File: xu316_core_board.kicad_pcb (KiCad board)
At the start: 4 copper layers, 53.3 x 68.6 mm, 120 parts, among them CN1 HX JN1.27-2x10P ZZ H4.9, J1 Conn_01x08, J10 Conn_02x04_Odd_Even, J11 Conn_01x03, J12 Conn_02x04_Odd_Even, J13 Conn_02x05_Odd_Even, J14 Conn_01x02, J15 Jack-DC, J16 Conn_02x06_Odd_Even, J17 Conn_01x03, J2 Conn_01x06, J3 Conn_01x10, J4 Conn_01x08, J5 Conn_01x03, J6 Conn_01x04, J7 Conn_02x04_Odd_Even, J8 Conn_01x02, J9 Conn_02x05_Odd_Even, Q1 SI1024X, SW1 RESET, SW3 SW_Push, SW4 SW_Push, SW5 SW_Push, SW6 SW_Push, U1 XU316-1024-QF60A-C32, U3 TPS62A0569PDRLR, U4 TPS62402DRCR, U5 LMR51450, U7 NUP4114, U8 W25Q32JVSS, Y2 24MHz

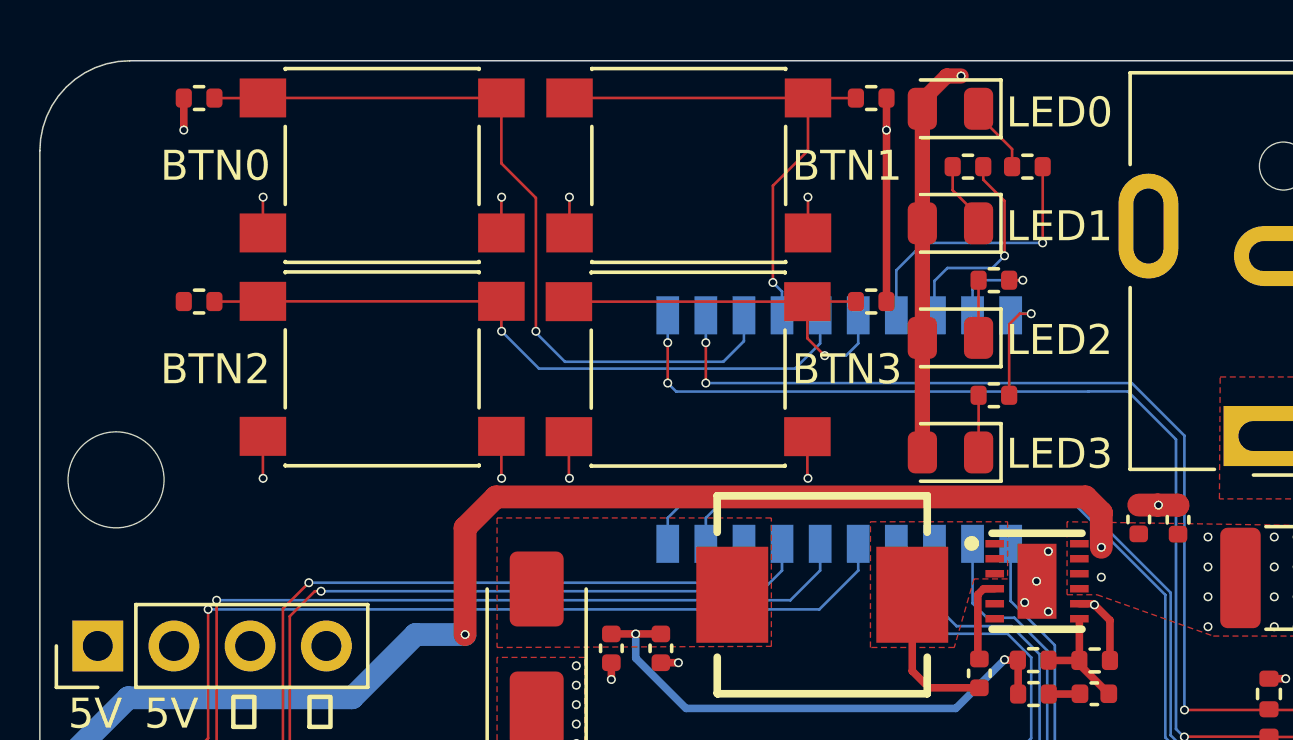
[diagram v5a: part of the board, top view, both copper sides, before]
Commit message: Added XMOS logo
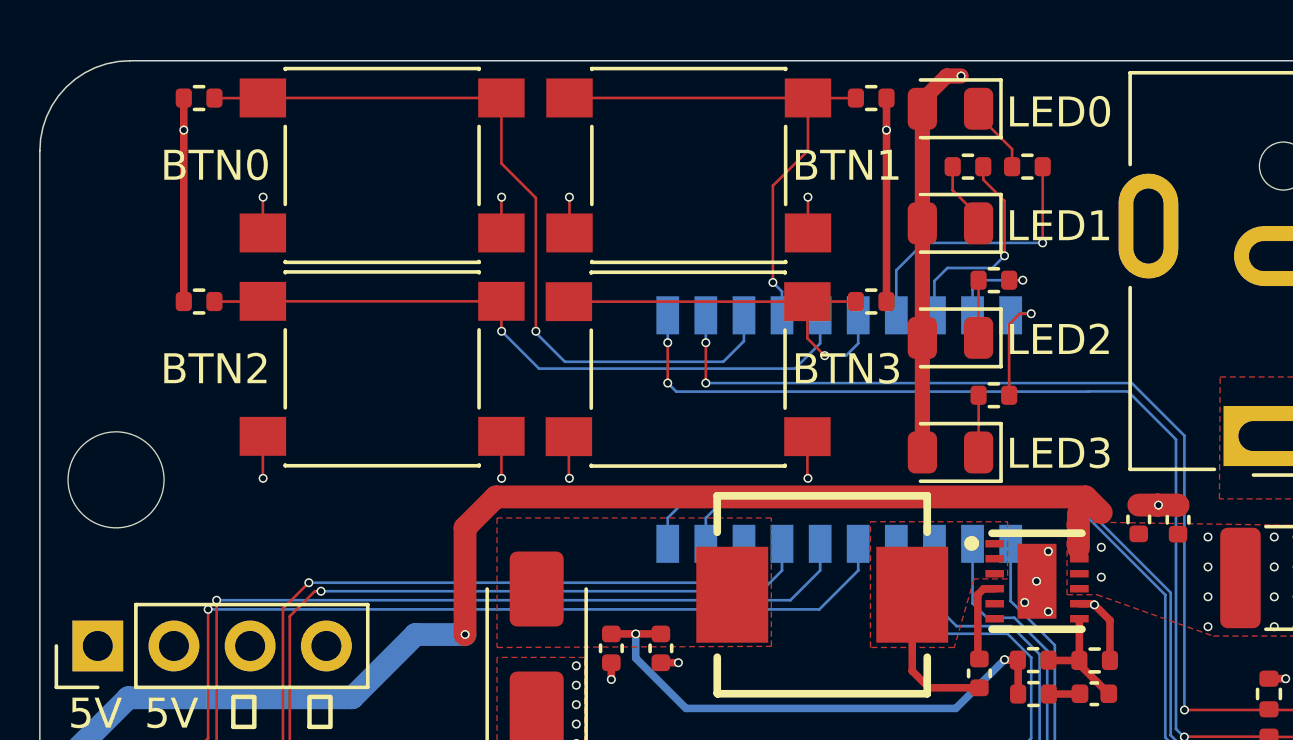
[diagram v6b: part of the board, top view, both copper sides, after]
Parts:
- added G***: LOGO, LOGO, B.Cu at (106.9, 46.4)
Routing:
- net VDDIO: track 96.5 -> 102.2 mm
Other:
- board text added: "CAE Generic PoC Module Board Rev 1.0"

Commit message: Ready to production
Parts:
- removed C35: 33U, Capacitor_SMD:C_0402_1005Metric
- C24: footprint Capacitor_SMD:C_0402_1005Metric -> Capacitor_SMD:C_0603_1608Metric
- C34: footprint Capacitor_SMD:C_0402_1005Metric -> Capacitor_SMD:CP_Elec_4x5.4
- moved C29 12.6 mm to (112.9, 100.1)
- moved C28 7.10 mm to (112.9, 98.9), turned to 180 degrees
- moved D2 2.11 mm to (111.9, 61.7)
- moved R20 1.63 mm to (112.9, 101.3)
- moved R19 1.51 mm to (112.9, 102.5)
- moved C27 1.49 mm to (137.8, 101.1), turned to 90 degrees
- moved R11 1.07 mm to (136.7, 101.1)
- moved C15 0.70 mm to (124.7, 89.2)
- moved C34 0.43 mm to (116.2, 62.0)
- moved C24 0.41 mm to (126.5, 93.0)
- moved C18 0.21 mm to (125.9, 78.1)
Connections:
- CN1 pad 1: +1.8V -> /TMS
- CN1 pad 10: /RST_N -> GND
- CN1 pad 11: VDDIO -> /XL_DN1
- CN1 pad 12: /XL_DN1 -> VDDIO
- CN1 pad 13: GND -> /XL_DN0
- CN1 pad 14: /XL_DN0 -> GND
- CN1 pad 15: GND -> /XL_UP0
- CN1 pad 16: /XL_UP0 -> GND
- CN1 pad 17: GND -> /XL_UP1
- CN1 pad 18: /XL_UP1 -> GND
- CN1 pad 19: GND -> unconnected-(CN1-Pad19)
- CN1 pad 2: /TMS -> +1.8V
- CN1 pad 20: unconnected-(CN1-Pad20) -> GND
- CN1 pad 3: GND -> /TCK
- CN1 pad 4: /TCK -> GND
- CN1 pad 5: GND -> /TDO
- CN1 pad 6: /TDO -> GND
- CN1 pad 7: GND -> /TDI
- CN1 pad 8: /TDI -> GND
- CN1 pad 9: GND -> /RST_N
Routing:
- net VDDIO: track 102.2 -> 113.9 mm
- net /XL_DN1: track 29.2 -> 23.6 mm
- net /X0P16B8: track 25.0 -> 29.0 mm, vias 1 -> 2
- net /XL_DN0: track 29.3 -> 25.3 mm
- net /RST_N: track 115.1 -> 118.9 mm
- net DCDC_5V: track 17.7 -> 14.2 mm
- net /XL_UP0: track 23.9 -> 21.0 mm
- net /TMS: track 17.3 -> 15.1 mm
- net +1.8V: track 154.2 -> 156.2 mm, vias 13 -> 12
- net /X0P16B12: track 40.2 -> 38.2 mm
- net /XL_UP1: track 23.4 -> 21.5 mm
- net /TDO: track 14.8 -> 12.8 mm
- net /TCK: track 16.9 -> 15.1 mm
- net /TDI: track 12.6 -> 10.9 mm
- net +5V(CORE): track 14.3 -> 15.9 mm, vias 4 -> 3
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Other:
- board text added: "CORE"
- board text added: "IO"

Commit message: Updated for manufacture
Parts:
- C21: footprint Capacitor_SMD:C_0402_1005Metric -> Capacitor_SMD:C_0603_1608Metric
- C30: footprint Capacitor_SMD:C_0402_1005Metric -> Capacitor_SMD:C_1206_3216Metric
- J15: footprint Connector_BarrelJack:BarrelJack_CUI_PJ-063AH_Horizontal -> Connector_BarrelJack:BarrelJack_GCT_DCJ200-10-A_Horizontal
- moved C30 3.88 mm to (134.8, 61.2), turned to -90 degrees
- moved J15 0.81 mm to (139.7, 54.5)
- moved C31 0.58 mm to (134.8, 57.3)
- moved C21 0.37 mm to (131.1, 76.0)
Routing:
- net +Vin: track 65.0 -> 64.2 mm
- net /IO Headers/SCL_XMOS: track 34.3 -> 33.6 mm
- net /IO Headers/SDA_XMOS: track 33.8 -> 33.2 mm
- net GND: track 39.7 -> 40.2 mm, vias 78 -> 79
- net +5V(IO): vias 5 -> 4
- net +5V(CORE): vias 3 -> 2
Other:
- board text added: "5.5-12V"
